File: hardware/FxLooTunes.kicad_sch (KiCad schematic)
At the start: 59 parts, among them J1 USB_C_Receptacle_USB2.0_16P, J2 AudioJack4, J3 USB_OUT, J4 Micro_SD_Card_Det1, J5 Prog, Q1 Si2301 A1SHB, Q2 Si2302 A2SHB, SW1 SW_Push, SW2 SW_Push, U1 XC6206PxxxMR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

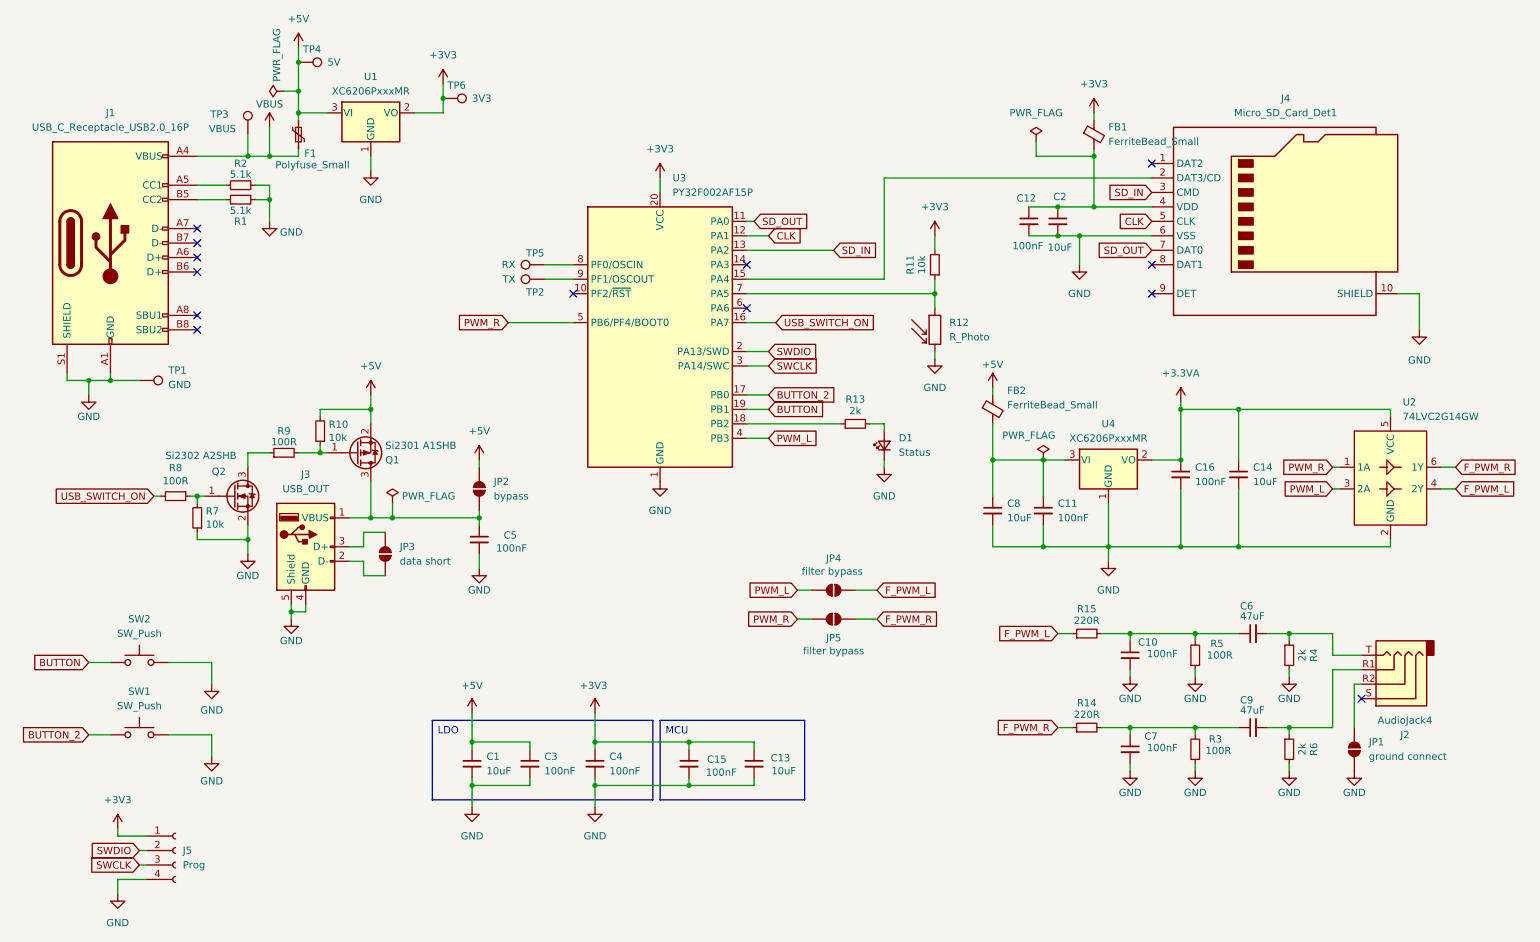
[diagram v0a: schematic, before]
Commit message: update schematics, remove watchdog remainings and workarounds
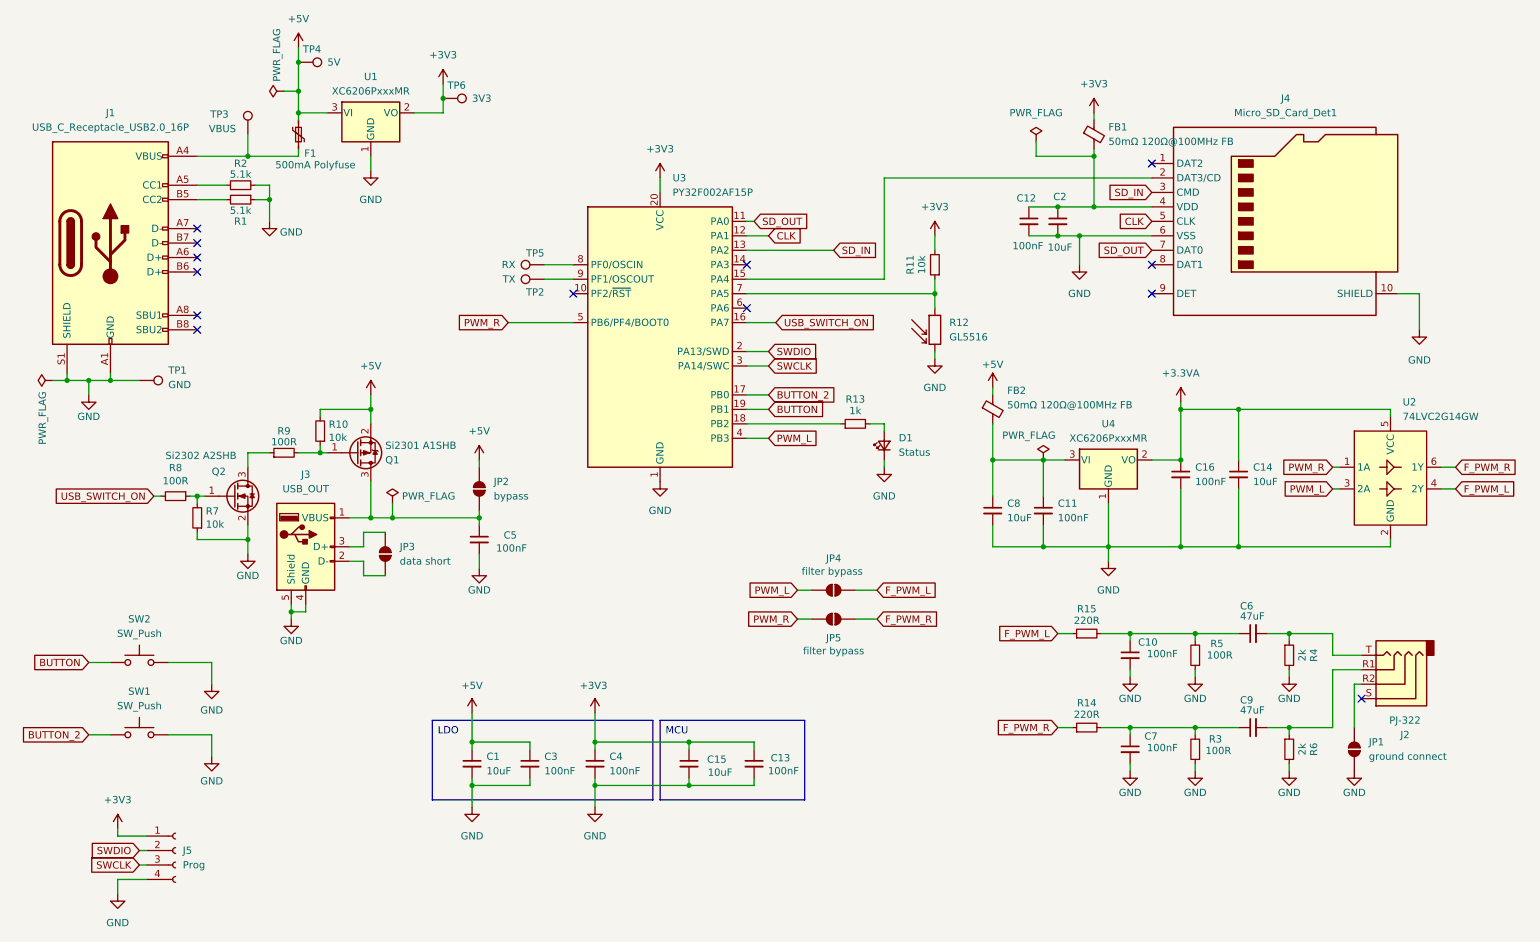
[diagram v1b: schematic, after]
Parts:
- C13: value 10uF -> 100nF
- C15: value 100nF -> 10uF
- F1: value Polyfuse_Small -> 500mA Polyfuse
- FB1, FB2: value FerriteBead_Small -> 50mΩ 120Ω@100MHz FB
- J2: value AudioJack4 -> PJ-322
- R12: value R_Photo -> GL5516
- R13: value 2k -> 1k
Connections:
- net VBUS: no longer names the net of F1.2, J1.A4 (VBUS), J1.A9 (VBUS), J1.B4 (VBUS), J1.B9 (VBUS), TP3.1
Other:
- company: (none) -> FxDev.pl
- title: (none) -> LooTunes
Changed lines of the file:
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@@
 	(generator_version "9.0")
 	(paper "A4")
+	(title_block
+		(title "LooTunes")
+		(company "FxDev.pl")
+	)
 	(text_box "LDO"
 		(exclude_from_sim no)
@@
 	)
 	(junction
+		(at 26.67 82.55)
+		(diameter 0)
+		(color 0 0 0 0)
+	)
+	(junction
 		(at 232.41 87.63)
 		(diameter 0)
@@
 		(color 0 0 0 0)
 	)
-	(junction
-		(at 62.23 43.18)
-		(diameter 0)
-		(color 0 0 0 0)
-	)
 	(no_connect
 		(at 146.05 69.85)
@@
 	(wire
 		(pts
+			(xy 24.13 82.55) (xy 26.67 82.55)
+		)
+		(stroke
+			(width 0)
+			(type default)
+		)
+	)
+	(wire
+		(pts
 			(xy 248.92 130.81) (xy 254 130.81)
 		)
@@
 	(wire
 		(pts
-			(xy 62.23 43.18) (xy 62.23 38.1)
-		)
-		(stroke
-			(width 0)
-			(type default)
-		)
-	)
-	(wire
-		(pts
 			(xy 198.12 96.52) (xy 198.12 102.87)
 		)
@@
 	(wire
 		(pts
-			(xy 58.42 43.18) (xy 62.23 43.18)
+			(xy 58.42 43.18) (xy 67.31 43.18)
 		)
 		(stroke
@@
 	(wire
 		(pts
-			(xy 62.23 43.18) (xy 67.31 43.18)
-		)
-		(stroke
-			(width 0)
-			(type default)
-		)
-	)
-	(wire
-		(pts
 			(xy 146.05 72.39) (xy 151.13 72.39)
 		)
@@
 			)
 		)
-		(property "Value" "R_Photo"
+		(property "Value" "GL5516"
 			(at 181.61 74.9299 0)
 			(effects
@@
 			)
 		)
-		(property "Value" "AudioJack4"
+		(property "Value" "PJ-322"
 			(at 261.62 142.24 0)
 			(effects
@@
 			)
 		)
-		(property "Value" "2k"
+		(property "Value" "1k"
 			(at 165.1 87.884 90)
 			(effects
@@
 			)
 		)
-		(property "Description" ""
+		(property "Description" "Unpolarized capacitor, small symbol"
 			(at 213.36 147.32 0)
 			(effects
@@
 			)
 		)
-		(property "Description" ""
+		(property "Description" "Unpolarized capacitor, small symbol"
 			(at 99.06 110.49 0)
 			(effects
@@
 	)
 	(symbol
+		(lib_id "power:PWR_FLAG")
+		(at 24.13 82.55 90)
+		(unit 1)
+		(exclude_from_sim no)
+		(in_bom yes)
+		(on_board yes)
+		(dnp no)
+		(property "Reference" "#U04"
+			(at 22.225 82.55 0)
+			(effects
+				(font
+					(size 1.27 1.27)
+				)
+				(hide yes)
+			)
+		)
+		(property "Value" "PWR_FLAG"
+			(at 22.352 89.154 0)
+			(effects
+				(font
+					(size 1.27 1.27)
+				)
+			)
+		)
+		(property "Footprint" ""
+			(at 24.13 82.55 0)
+			(effects
+				(font
+					(size 1.27 1.27)
+				)
+				(hide yes)
+			)
+		)
+		(property "Datasheet" "~"
+			(at 24.13 82.55 0)
+			(effects
+				(font
+					(size 1.27 1.27)
+				)
+				(hide yes)
+			)
+		)
+		(property "Description" "Special symbol for telling ERC where power comes from"
+			(at 24.13 82.55 0)
+			(effects
+				(font
+					(size 1.27 1.27)
+				)
+				(hide yes)
+			)
+		)
+		(pin "1"
+		)
+		(instances
+			(project "FxLooTunes"
+				(path "/97c1ba9b-17a9-4b43-8bd2-d73582c7b037"
+					(reference "#U04")
+					(unit 1)
+				)
+			)
+		)
+	)
+	(symbol
 		(lib_id "power:GND")
 		(at 99.06 115.57 0)
@@
 			)
 		)
-		(property "Description" ""
+		(property "Description" "Power symbol creates a global label with name \"GND\" , ground"
 			(at 99.06 115.57 0)
 			(effects
@@
 			)
 		)
-		(property "Description" ""
+		(property "Description" "-4.4A Id, -40V Vds, P-Channel MOSFET, SOT-23"
 			(at 77.47 95.25 0)
 			(effects
@@
 			)
 		)
-		(property "Value" "100nF"
-			(at 144.272 151.384 0)
+		(property "Value" "10uF"
+			(at 143.51 151.384 0)
 			(effects
 				(font
@@
 			)
 		)
-		(property "Description" ""
+		(property "Description" "Unpolarized capacitor, small symbol"
 			(at 135.89 149.86 0)
 			(effects
@@
 			)
 		)
-		(property "Value" "FerriteBead_Small"
+		(property "Value" "50mΩ 120Ω@100MHz FB"
 			(at 209.55 40.6018 0)
 			(effects
@@
 			)
 		)
-		(property "Description" ""
+		(property "Description" "Unpolarized capacitor, small symbol"
 			(at 213.36 130.81 0)
 			(effects
@@
 			)
 		)
-		(property "Value" "10uF"
-			(at 154.686 151.13 0)
+		(property "Value" "100nF"
+			(at 155.194 151.13 0)
 			(effects
 				(font
@@
 			)
 		)
-		(property "Description" ""
+		(property "Description" "Unpolarized capacitor, small symbol"
 			(at 147.32 149.86 0)
 			(effects
@@
 			)
 		)
-		(property "Description" ""
+		(property "Description" "Resistor, small symbol"
 			(at 57.15 48.26 0)
 			(effects
@@
 			)
 		)
-		(property "Value" "Polyfuse_Small"
+		(property "Value" "500mA Polyfuse"
 			(at 63.246 44.704 0)
 			(effects
@@
 			)
 		)
-		(property "Description" ""
+		(property "Description" "Resistor, small symbol"
 			(at 64.77 95.25 0)
 			(effects
@@
 			)
 		)
-		(property "Description" ""
+		(property "Description" "Resistor, small symbol"
 			(at 49.53 106.68 0)
 			(effects
@@
 			)
 		)
-		(property "Description" ""
+		(property "Description" "Special symbol for telling ERC where power comes from"
 			(at 83.82 104.14 0)
 			(effects
@@
 			)
 		)
-		(property "Description" ""
+		(property "Description" "Resistor, small symbol"
 			(at 45.72 102.87 0)
 			(effects
@@
 			)
 		)
-		(property "Value" "FerriteBead_Small"
+		(property "Value" "50mΩ 120Ω@100MHz FB"
 			(at 191.77 86.868 0)
 			(effects
@@
 			)
 		)
-		(property "Description" ""
+		(property "Description" "Power symbol creates a global label with name \"GND\" , ground"
 			(at 30.48 85.09 0)
 			(effects
@@
 			)
 		)
-		(property "Description" ""
+		(property "Description" "USB Type A connector"
 			(at 68.58 111.76 0)
 			(effects
@@
 			)
 		)
-		(property "Description" ""
+		(property "Description" "Special symbol for telling ERC where power comes from"
 			(at 64.77 31.75 0)
 			(effects
@@
 			)
 		)
-		(property "Description" ""
+		(property "Description" "Resistor, small symbol"
 			(at 71.12 91.44 0)
 			(effects
@@
 			)
 		)
-		(property "Description" ""
+		(property "Description" "Unpolarized capacitor, small symbol"
 			(at 234.95 143.51 0)
 			(effects
@@
 			)
 		)
-		(property "Description" ""
+		(property "Description" "Resistor, small symbol"
 			(at 57.15 50.8 0)
 			(effects
@@
 			)
 		)
-		(property "Description" ""
+		(property "Description" "Power symbol creates a global label with name \"GND\" , ground"
 			(at 66.04 124.46 0)
 			(effects
@@
 			)
 		)
-		(property "Description" ""
+		(property "Description" "Power symbol creates a global label with name \"GND\" , ground"
 			(at 58.42 113.03 0)
 			(effects
@@
 	)
 	(symbol
-		(lib_id "power:VBUS")
-		(at 62.23 38.1 0)
-		(unit 1)
-		(exclude_from_sim no)
-		(in_bom yes)
-		(on_board yes)
-		(dnp no)
-		(property "Reference" "#PWR04"
-			(at 62.23 41.91 0)
-			(effects
-				(font
-					(size 1.27 1.27)
-				)
-				(hide yes)
-			)
-		)
-		(property "Value" "VBUS"
-			(at 62.23 34.036 0)
-			(effects
-				(font
-					(size 1.27 1.27)
-				)
-			)
-		)
-		(property "Footprint" ""
-			(at 62.23 38.1 0)
-			(effects
-				(font
-					(size 1.27 1.27)
-				)
-				(hide yes)
-			)
-		)
-		(property "Datasheet" ""
-			(at 62.23 38.1 0)
-			(effects
-				(font
-					(size 1.27 1.27)
-				)
-				(hide yes)
-			)
-		)
-		(property "Description" "Power symbol creates a global label with name \"VBUS\""
-			(at 62.23 38.1 0)
-			(effects
-				(font
-					(size 1.27 1.27)
-				)
-				(hide yes)
-			)
-		)
-		(pin "1"
-		)
-		(instances
-			(project "FxLooTunes"
-				(path "/97c1ba9b-17a9-4b43-8bd2-d73582c7b037"
-					(reference "#PWR04")
-					(unit 1)
-				)
-			)
-		)
-	)
-	(symbol
 		(lib_id "power:PWR_FLAG")
 		(at 198.12 96.52 0)
@@
 			)
 		)
-		(property "Description" ""
+		(property "Description" "Special symbol for telling ERC where power comes from"
 			(at 198.12 96.52 0)
 			(effects
@@
 			)
 		)
-		(property "Description" ""
+		(property "Description" "Unpolarized capacitor, small symbol"
 			(at 200.66 54.61 0)
 			(effects
@@
 			)
 		)
-		(property "Description" ""
+		(property "Description" "Power symbol creates a global label with name \"GND\" , ground"
 			(at 62.23 54.61 0)
 			(effects
@@
 			)
 		)
-		(property "Description" ""
+		(property "Description" "Unpolarized capacitor, small symbol"
 			(at 195.58 54.61 0)
 			(effects
@@
 			)
 		)
-		(property "Description" ""
+		(property "Description" "0.115A Id, 60V Vds, N-Channel MOSFET, SOT-23"
 			(at 55.88 102.87 0)
 			(effects
@@
 			)
 		)
-		(property "Description" ""
+		(property "Description" "Unpolarized capacitor, small symbol"
 			(at 234.95 127 0)
 			(effects
